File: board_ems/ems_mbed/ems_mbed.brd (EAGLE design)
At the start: 87 x 107 mm, 146 parts, among them IC1 SIM900, IC2 74HC595D, IC3 74HC595D, IC4 ADE7758RW, J5 POWER_JACKPTH, U2 W5500

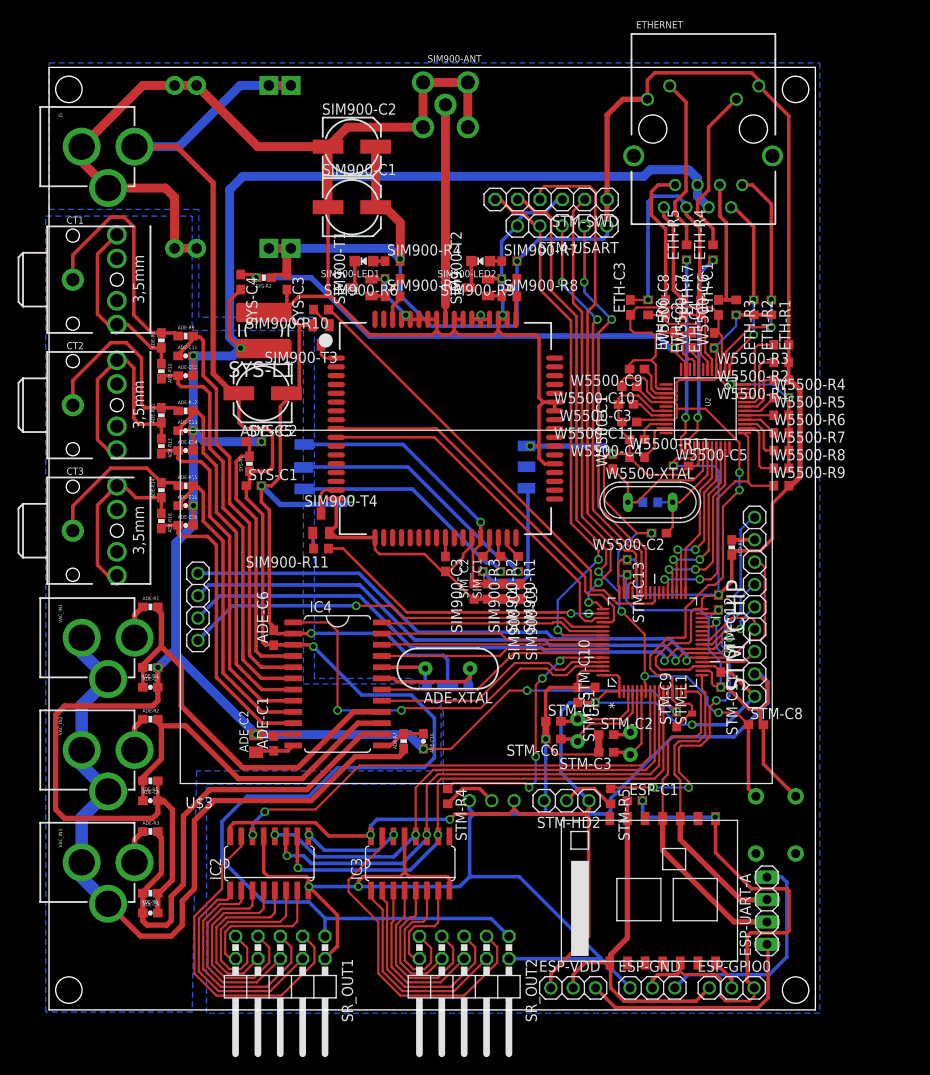
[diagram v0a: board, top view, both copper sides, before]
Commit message: add dht, mq6, and mq7 sensors
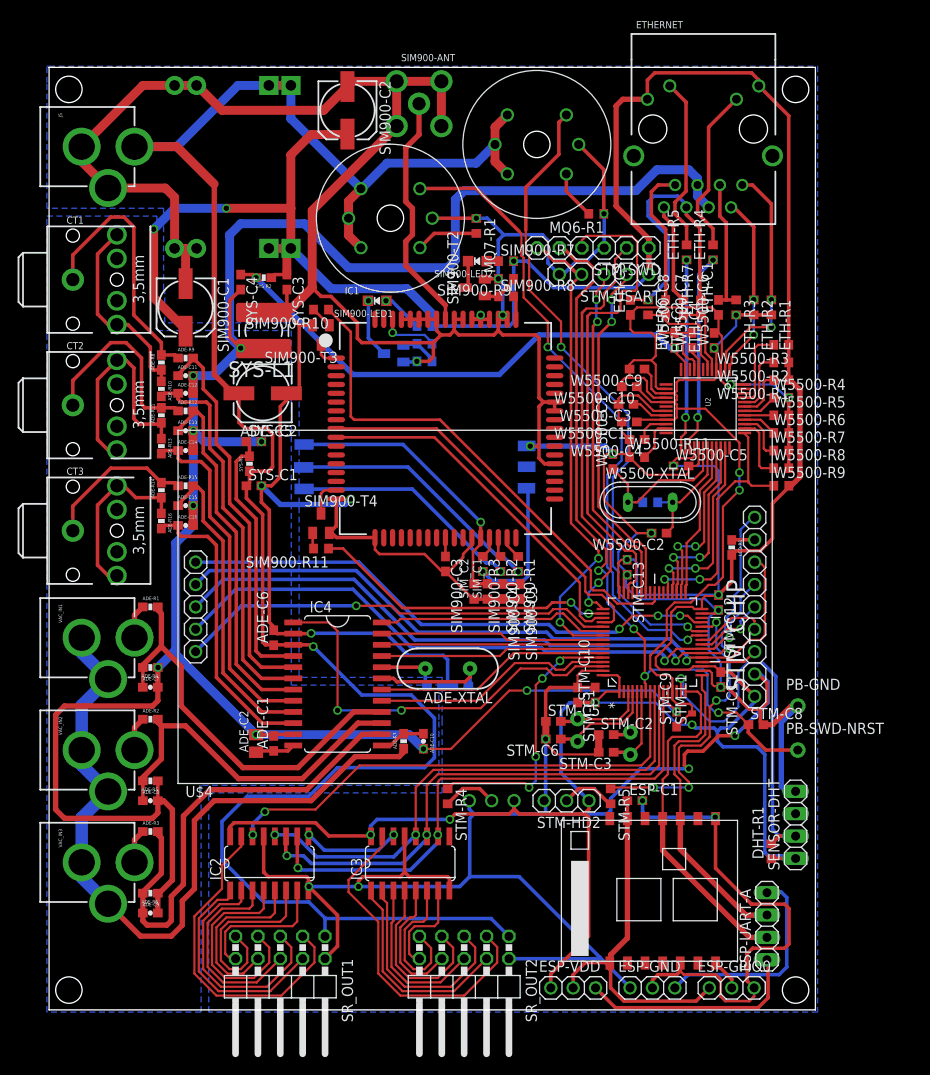
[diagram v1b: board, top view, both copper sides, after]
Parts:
- removed STM-S2: SWITCH-MOMENTARY-2PTH, SparkFun-Electromechanical:TACTILE-PTH
- removed U$3: TFT_LCD_2.2, TFT_LCD_2.2:TFT_LCD_2.2
- added DHT-R1, MQ6-R1, MQ7-R1: 10k, resistor:R0603
- added PB-GND, PB-SWD-NRST: (no value), adafruit:1X01-CLEANBIG
- added SENSOR-DHT: (no value), pinhead:1X04
- added SENSOR-MQ6, SENSOR-MQ7: METHANE_SENSOR, SparkFun-Sensors:MQ-3
- added U$4: TFT_LCD_2.2+F_CS, TFT_LCD_2.2:TFT_LCD_2.2+F_CS
- moved SIM900-C1 22.0 mm to (-71.5, 79.8), turned to 270 degrees
- moved SIM900-R6 10.1 mm to (-44.4, 73.6), flipped to the bottom, turned to 0 degrees
- moved SIM900-T1 8.33 mm to (-47.9, 74.5), flipped to the bottom, turned to 270 degrees
- moved SIM900-R4 8.22 mm to (-44.4, 77.6), flipped to the bottom, turned to 180 degrees
- moved STM-SWD 7.27 mm to (-25.2, 86.5)
- moved STM-USART 7.27 mm to (-24.0, 83.5)
- moved SIM900-R5 6.48 mm to (-44.4, 75.6), flipped to the bottom, turned to 180 degrees
- moved SIM900-LED1 4.74 mm to (-49.8, 80.5)
- moved SIM900-C2 4.16 mm to (-53.1, 102.1), turned to 270 degrees
- moved SIM900-ANT 3.00 mm to (-45.0, 102.9)
- moved ADE-R8 2.50 mm to (-74.2, 73.5)
- moved ADE-R9 2.50 mm to (-71.5, 74.0)
- moved ADE-C11 2.25 mm to (-71.5, 72.0)
- moved ADE-C12 2.00 mm to (-71.5, 70.0)
- moved ADE-R10 2.00 mm to (-74.2, 70.5)
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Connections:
- new net DHT_DATA: DHT-R1.2, SENSOR-DHT.2, STM_CHIP.15
- new net F_CS: STM_CHIP.29, U$4.F_CS
- new net MQ6_DATA: SENSOR-MQ7.B1, STM_CHIP.26
- new net MQ7_DATA: SENSOR-MQ6.B1, STM_CHIP.27
- new net N$43: MQ7-R1.2, SENSOR-MQ7.B2
- new net N$9: MQ6-R1.2, SENSOR-MQ6.B2
- net +5V: now also SENSOR-MQ6.A1, SENSOR-MQ6.A2, SENSOR-MQ6.HA, SENSOR-MQ7.A1, SENSOR-MQ7.A2, SENSOR-MQ7.HA
- net DGND: now also MQ6-R1.1, MQ7-R1.1, PB-GND.1, SENSOR-DHT.4, SENSOR-MQ6.HB, SENSOR-MQ7.HB, U$4.LCD_GND; no longer STM-S2.3, U$3.LCD_GND
- net LCD_CS: now also U$4.LCD_CS; no longer U$3.LCD_CS
- net LCD_D/C: now also U$4.LCD_D/C; no longer U$3.LCD_D/C
- net LCD_LED: now also U$4.LCD_LED; no longer U$3.LCD_LED
- net LCD_MISO: now also U$4.LCD_MISO, U$4.SD_MISO; no longer U$3.LCD_MISO, U$3.SD_MISO
- net LCD_MOSI: now also U$4.LCD_MOSI, U$4.SD_MOSI; no longer U$3.LCD_MOSI, U$3.SD_MOSI
- net LCD_RESET: now also U$4.LCD_RESET; no longer U$3.LCD_RESET
- net LCD_SCK: now also U$4.LCD_SCK, U$4.SD_SCK; no longer U$3.LCD_SCK, U$3.SD_SCK
- net SD_CS: now also U$4.SD_CS; no longer U$3.SD_CS
- net SWD_NRST: now also PB-SWD-NRST.1; no longer STM-S2.1
- net VDD: now also DHT-R1.1, SENSOR-DHT.1, U$4.LCD_VCC; no longer U$3.LCD_VCC
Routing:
- net MQ7_DATA: track 0.00 -> 73.2 mm, vias 0 -> 2
- net MQ6_DATA: track 0.00 -> 72.8 mm, vias 0 -> 2
- net VDD: track 361.2 -> 429.3 mm, vias 10 -> 11
- net F_CS: track 0.00 -> 61.9 mm, vias 0 -> 3
- net +5V: track 188.7 -> 236.7 mm
- net DGND: track 669.2 -> 714.1 mm, vias 18 -> 21
- net DHT_DATA: track 0.00 -> 44.5 mm, vias 0 -> 1
- net SWD_SWO: track 62.2 -> 54.9 mm
- net N$43: track 0.00 -> 7.07 mm
- net SERIAL_RX: track 46.2 -> 39.5 mm
- net SERIAL_TX: track 46.2 -> 40.0 mm
- net SIM_PWRKEY: track 53.1 -> 58.9 mm
- net N$9: track 0.00 -> 5.58 mm
- net SWD_NRST: track 86.6 -> 82.0 mm
- net N$17: track 3.12 -> 7.34 mm, vias 0 -> 1
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
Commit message: add grber, chg ems_mbed w/ corct ones, del oth file
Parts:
- removed DHT-R1, MQ6-R1, MQ7-R1: 10k, resistor:R0603
- removed PB-GND, PB-SWD-NRST: (no value), adafruit:1X01-CLEANBIG
- removed SENSOR-DHT: (no value), pinhead:1X04
- removed SENSOR-MQ6, SENSOR-MQ7: METHANE_SENSOR, SparkFun-Sensors:MQ-3
- removed U$4: TFT_LCD_2.2+F_CS, TFT_LCD_2.2:TFT_LCD_2.2+F_CS
- added STM-S2: SWITCH-MOMENTARY-2PTH, SparkFun-Electromechanical:TACTILE-PTH
- added U$3: TFT_LCD_2.2, TFT_LCD_2.2:TFT_LCD_2.2
- moved SIM900-C1 22.0 mm to (-52.6, 91.1), turned to 0 degrees
- moved SIM900-R6 10.1 mm to (-48.0, 83.0), flipped to the top, turned to 180 degrees
- moved SIM900-T1 8.33 mm to (-51.5, 82.0), flipped to the top, turned to 90 degrees
- moved SIM900-R4 8.22 mm to (-48.0, 85.0), flipped to the top, turned to 0 degrees
- moved STM-SWD 7.27 mm to (-30.0, 92.0)
- moved STM-USART 7.27 mm to (-28.8, 89.0)
- moved SIM900-R5 6.48 mm to (-48.0, 81.0), flipped to the top, turned to 0 degrees
- moved SIM900-LED1 4.74 mm to (-51.2, 85.0)
- moved SIM900-C2 4.16 mm to (-52.6, 98.0), turned to 0 degrees
- moved SIM900-ANT 3.00 mm to (-42.0, 102.8)
- moved ADE-R8 2.50 mm to (-74.2, 76.0)
- moved ADE-R9 2.50 mm to (-71.5, 76.5)
- moved ADE-C11 2.25 mm to (-71.5, 74.2)
- moved ADE-C12 2.00 mm to (-71.5, 72.0)
- moved ADE-R10 2.00 mm to (-74.2, 72.5)
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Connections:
- removed net DHT_DATA: DHT-R1.2, SENSOR-DHT.2, STM_CHIP.15
- removed net F_CS: STM_CHIP.29, U$4.F_CS
- removed net MQ6_DATA: SENSOR-MQ7.B1, STM_CHIP.26
- removed net MQ7_DATA: SENSOR-MQ6.B1, STM_CHIP.27
- removed net N$43: MQ7-R1.2, SENSOR-MQ7.B2
- removed net N$9: MQ6-R1.2, SENSOR-MQ6.B2
- net +5V: no longer SENSOR-MQ6.A1, SENSOR-MQ6.A2, SENSOR-MQ6.HA, SENSOR-MQ7.A1, SENSOR-MQ7.A2, SENSOR-MQ7.HA
- net DGND: now also STM-S2.3, U$3.LCD_GND; no longer MQ6-R1.1, MQ7-R1.1, PB-GND.1, SENSOR-DHT.4, SENSOR-MQ6.HB, SENSOR-MQ7.HB, U$4.LCD_GND
- net LCD_CS: now also U$3.LCD_CS; no longer U$4.LCD_CS
- net LCD_D/C: now also U$3.LCD_D/C; no longer U$4.LCD_D/C
- net LCD_LED: now also U$3.LCD_LED; no longer U$4.LCD_LED
- net LCD_MISO: now also U$3.LCD_MISO, U$3.SD_MISO; no longer U$4.LCD_MISO, U$4.SD_MISO
- net LCD_MOSI: now also U$3.LCD_MOSI, U$3.SD_MOSI; no longer U$4.LCD_MOSI, U$4.SD_MOSI
- net LCD_RESET: now also U$3.LCD_RESET; no longer U$4.LCD_RESET
- net LCD_SCK: now also U$3.LCD_SCK, U$3.SD_SCK; no longer U$4.LCD_SCK, U$4.SD_SCK
- net SD_CS: now also U$3.SD_CS; no longer U$4.SD_CS
- net SWD_NRST: now also STM-S2.1; no longer PB-SWD-NRST.1
- net VDD: now also U$3.LCD_VCC; no longer DHT-R1.1, SENSOR-DHT.1, U$4.LCD_VCC
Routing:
- net MQ7_DATA: track 73.2 -> 0.00 mm, vias 2 -> 0
- net MQ6_DATA: track 72.8 -> 0.00 mm, vias 2 -> 0
- net VDD: track 429.3 -> 361.2 mm, vias 11 -> 10
- net F_CS: track 61.9 -> 0.00 mm, vias 3 -> 0
- net +5V: track 236.7 -> 188.7 mm
- net DGND: track 714.1 -> 669.2 mm, vias 21 -> 18
- net DHT_DATA: track 44.5 -> 0.00 mm, vias 1 -> 0
- net SWD_SWO: track 54.9 -> 62.2 mm
- net N$43: track 7.07 -> 0.00 mm
- net SERIAL_RX: track 39.5 -> 46.2 mm
- net SERIAL_TX: track 40.0 -> 46.2 mm
- net SIM_PWRKEY: track 58.9 -> 53.1 mm
- net N$9: track 5.58 -> 0.00 mm
- net SWD_NRST: track 82.0 -> 86.6 mm
- net N$17: track 7.34 -> 3.12 mm, vias 1 -> 0
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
